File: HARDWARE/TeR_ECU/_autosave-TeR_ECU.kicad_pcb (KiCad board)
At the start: 4 copper layers, 68 parts, among them IC1 MX34040NF2, J1 Debug, J2 RJ45_Shielded, J3 RJ45_Shielded, J4 RJ45_Shielded, Q1 ZXMN3F30FH, Q2 ZXMN3F30FH, SW1 RST, U1 STM32F446RETx, U2 SN65HVD230, U3 SN65HVD230, U4 LM1117MP-3.3, U5 TSR_1-2450, U6 TSR_1-24120, U7 HDSP-A153, Y1 Crystal

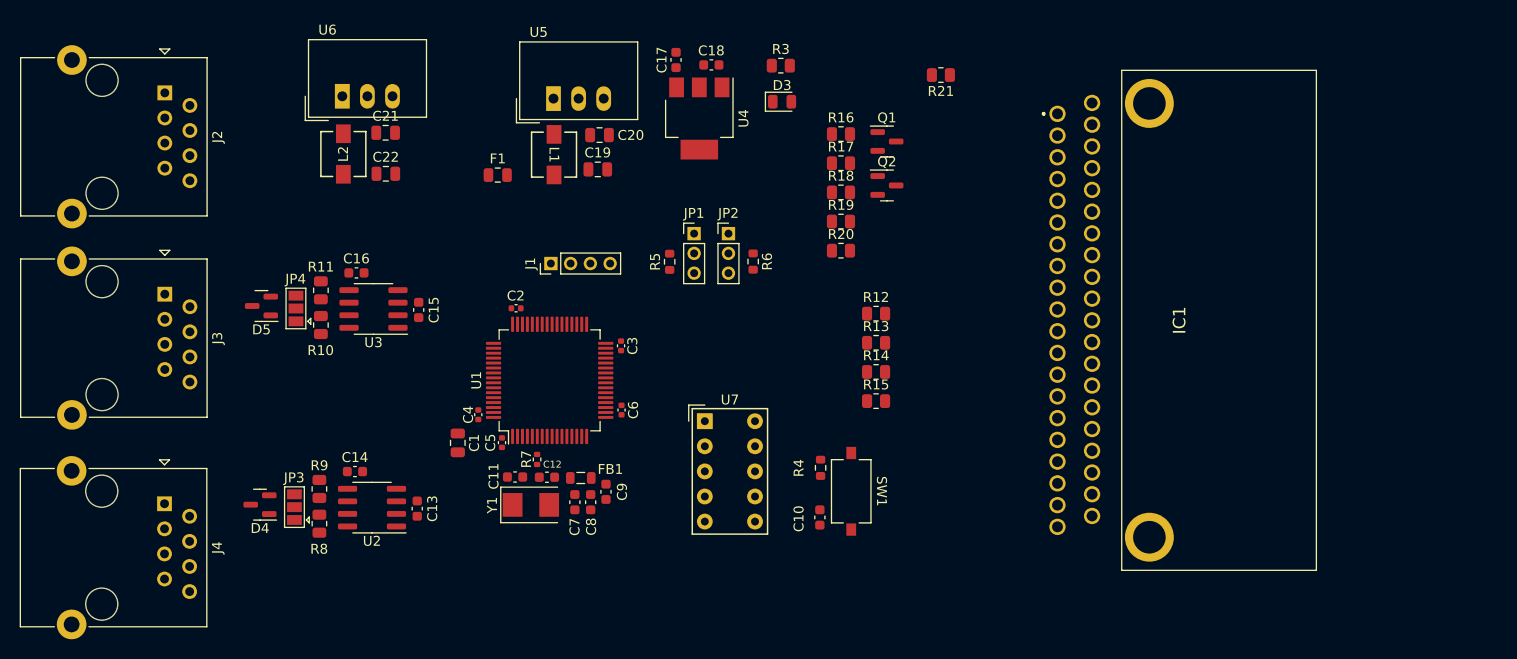
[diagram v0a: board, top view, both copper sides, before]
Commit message: Rethought layout and added pulldown to Horn mosfet
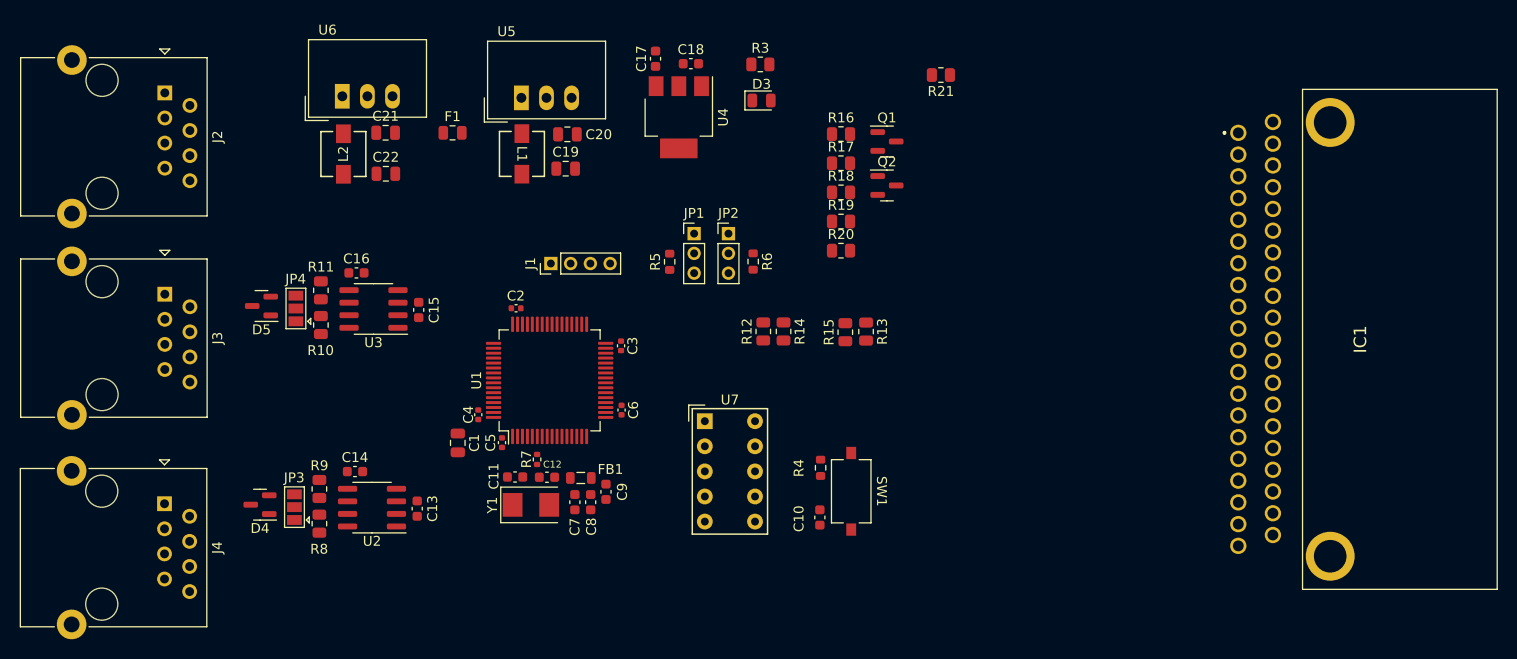
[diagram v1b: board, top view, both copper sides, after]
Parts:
- moved IC1 18.4 mm to (210.4, 67.8)
- moved R12 11.6 mm to (149.9, 67.0), turned to 90 degrees
- moved R14 10.2 mm to (152.0, 67.0), turned to -90 degrees
- moved R15 7.64 mm to (158.2, 67.0), turned to 90 degrees
- moved F1 6.26 mm to (118.5, 46.9)
- moved L1 3.25 mm to (125.5, 49.0)
- moved C20 3.25 mm to (130.1, 47.0)
- moved U5 3.25 mm to (125.5, 43.3)
- moved C19 3.25 mm to (129.9, 50.5)
- moved C17 2.08 mm to (139.0, 39.4)
- moved C18 2.08 mm to (142.6, 39.9)
- moved D3 2.08 mm to (149.8, 43.6)
- moved R3 2.08 mm to (149.7, 39.9)
- moved U4 2.08 mm to (141.4, 45.3)
- moved R13 1.52 mm to (160.3, 67.0), turned to -90 degrees
